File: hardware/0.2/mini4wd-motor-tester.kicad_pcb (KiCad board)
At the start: 4 copper layers, 100 x 48 mm, 116 parts, among them J1 USB_C_Receptacle_USB2.0_16P, J2 JST SH, J4 JST XH, M1 Motor_DC, M2 TP, M3 TP, Q2 AO3401A, Q3 2N7002, SW1 RA, SW2 RA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

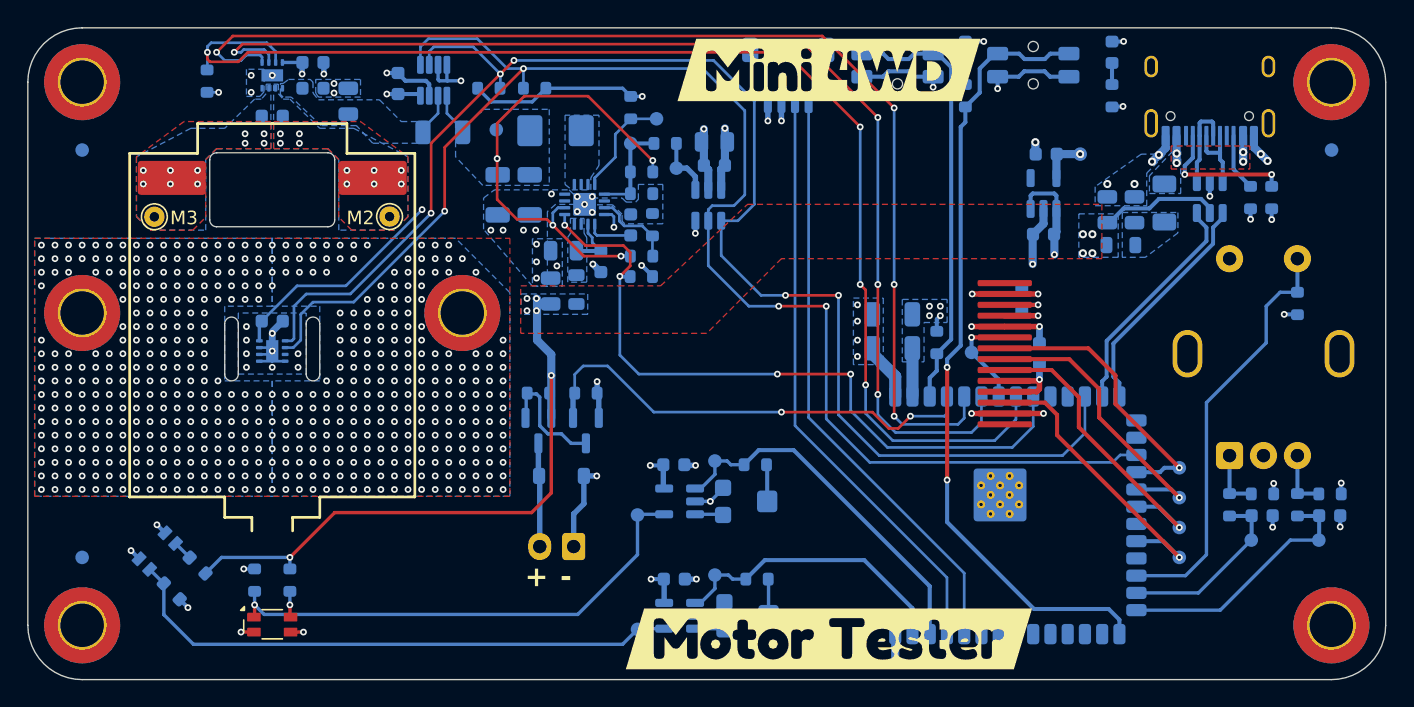
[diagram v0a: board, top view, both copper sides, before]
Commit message: add v2 heatsink, improve layout for v2 main
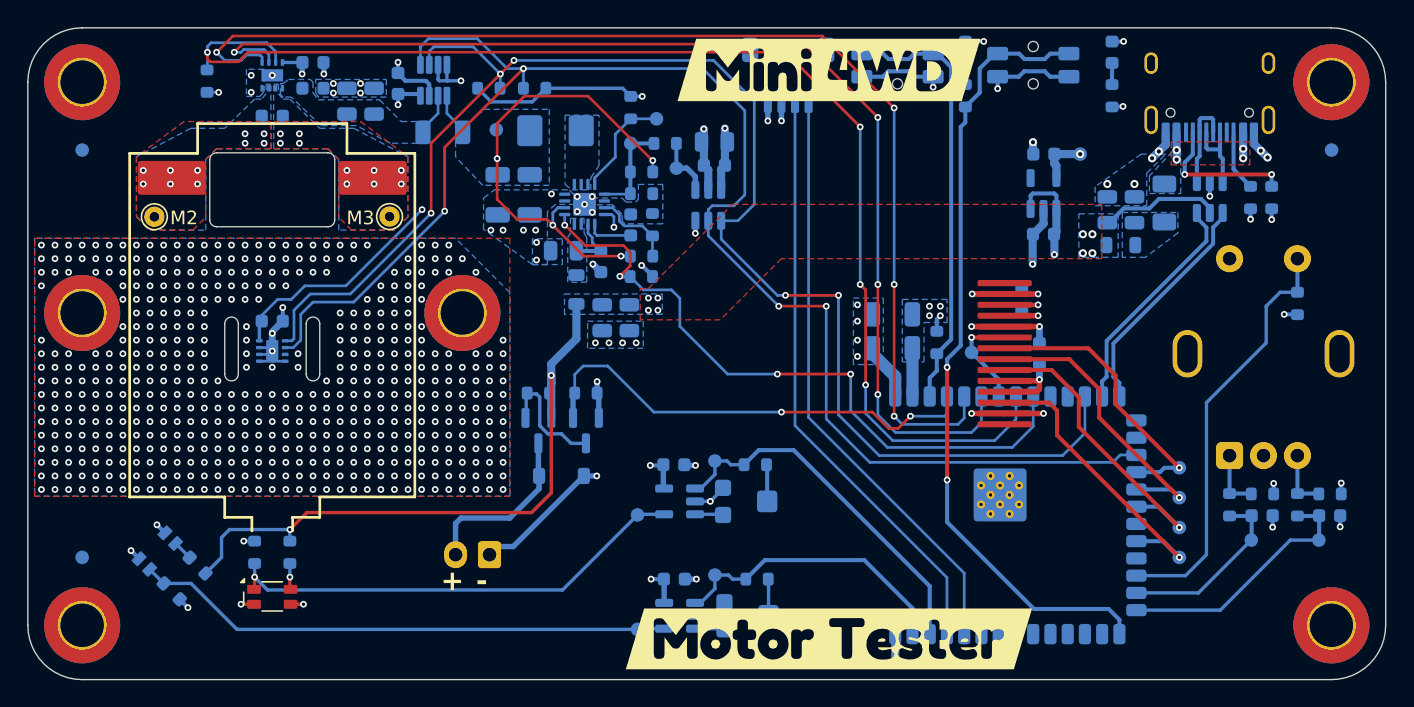
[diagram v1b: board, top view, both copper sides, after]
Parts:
- added C26: 10u, Capacitor_SMD:C_0805_2012Metric, B.Cu at (91.5, 81.4)
- added C27: 10u, Capacitor_SMD:C_0805_2012Metric, B.Cu at (110.3, 97.3)
- moved J4 6.23 mm to (100.0, 114.8)
- moved G1 6.17 mm to (86.8, 122.1)
- moved C1 4.28 mm to (108.3, 97.3), turned to -90 degrees
- moved R17 2.05 mm to (85.3, 114.6)
- moved R22 2.05 mm to (82.7, 114.6)
- moved U8 2.05 mm to (84.0, 118.0)
- moved J1 0.25 mm to (153.0, 79.7)
- moved C10 0.18 mm to (140.8, 85.3)
- moved C23 0.10 mm to (89.5, 81.4)
- renumbered M3 to M2, M2 to M3
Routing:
- net Net-(D3-K): track 7.64 -> 12.3 mm
- net GND: track 100.7 -> 105.3 mm, vias 594 -> 600
- net /REG_EN: track 52.8 -> 49.8 mm
- net Net-(U13--): track 37.1 -> 34.8 mm
- net Net-(U11--): track 42.0 -> 39.7 mm
- net +5V: track 63.1 -> 64.5 mm
- net /I2C_SCL: track 115.1 -> 113.8 mm
- net /I2C_SDA: track 111.5 -> 110.6 mm
- net +3V3: track 69.3 -> 69.8 mm
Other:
- board text added: "MINI4WD MOTOR TESTER REV 0.2"
- board text removed: "MINI4WD MOTOR TESTER REVISION 0.2"

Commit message: minor sch and pcb updates
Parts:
- moved D3 5.49 mm to (104.3, 114.4), turned to -90 degrees
- moved Q2 0.70 mm to (104.3, 105.7)
- moved Q3 0.70 mm to (107.8, 105.7)
- moved R27 0.70 mm to (107.8, 102.9)
- moved R28 0.70 mm to (104.3, 102.9)
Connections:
- C5 pad 1: Net-(C5-Pad1) -> Net-(U2-VBUS)
- F1 pad 2: Net-(C5-Pad1) -> Net-(U2-VBUS)
- FB2 pad 2: Net-(C5-Pad1) -> Net-(U2-VBUS)
- U2 pad 5: +5V -> Net-(U2-VBUS)
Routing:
- net +5V: track 64.5 -> 55.4 mm
- net +VMOT: track 37.2 -> 28.6 mm
- net Net-(U2-VBUS): track 0.00 -> 5.14 mm
- net GND: track 105.3 -> 100.7 mm
- net Net-(D3-K): track 12.3 -> 14.5 mm
- net Net-(J1-CC1): track 10.6 -> 12.3 mm
- net /REG_EN: track 49.8 -> 48.6 mm
- net /AUX_5V_EN: track 34.6 -> 33.9 mm
- added copper zone on B.Cu, net Net-(U2-VBUS)
- removed copper zone on B.Cu, net Net-(C5-Pad1)

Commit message: off to fab
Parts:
- R29, R32: value 180K -> 200K
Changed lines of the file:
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@@
 			)
 		)
-		(property "LCSC" ""
+		(property "LCSC" "C25803"
 			(at 0 0 0)
 			(unlocked yes)
@@
 			)
 		)
-		(property "MPN " ""
+		(property "MPN " "0603WAF1003T5E"
 			(at 0 0 0)
 			(unlocked yes)
@@
 			)
 		)
-		(property "LCSC" ""
+		(property "LCSC" "C4216"
 			(at 0 0 180)
 			(unlocked yes)
@@
 			)
 		)
-		(property "MPN " ""
+		(property "MPN " "0603WAF3302T5E"
 			(at 0 0 180)
 			(unlocked yes)
@@
 			)
 		)
-		(property "LCSC" ""
+		(property "LCSC" "C8218"
 			(at 0 0 270)
 			(unlocked yes)
@@
 			)
 		)
-		(property "MPN " ""
+		(property "MPN " "0603WAF2000T5E"
 			(at 0 0 270)
 			(unlocked yes)
@@
 			)
 		)
-		(property "Value" "180K"
+		(property "Value" "200K"
 			(at 0 -1.43 0)
 			(layer "B.Fab")
@@
 			)
 		)
+		(property "Manufacturer" "UNI-ROYAL"
+			(at 0 0 180)
+			(unlocked yes)
+			(layer "B.Fab")
+			(hide yes)
+			(effects
+				(font
+					(size 1 1)
+					(thickness 0.15)
+				)
+				(justify mirror)
+			)
+		)
+		(property "LCSC" "C25811"
+			(at 0 0 180)
+			(unlocked yes)
+			(layer "B.Fab")
+			(hide yes)
+			(effects
+				(font
+					(size 1 1)
+					(thickness 0.15)
+				)
+				(justify mirror)
+			)
+		)
+		(property "MPN " "0603WAF2003T5E"
+			(at 0 0 180)
+			(unlocked yes)
+			(layer "B.Fab")
+			(hide yes)
+			(effects
+				(font
+					(size 1 1)
+					(thickness 0.15)
+				)
+				(justify mirror)
+			)
+		)
 		(property ki_fp_filters "R_*")
 		(sheetname "/")
@@
 			)
 		)
-		(property "LCSC" ""
+		(property "LCSC" "C25819"
 			(at 0 0 90)
 			(unlocked yes)
@@
 			)
 		)
-		(property "MPN " ""
+		(property "MPN " "0603WAF4702T5E"
 			(at 0 0 90)
 			(unlocked yes)
@@
 			)
 		)
-		(property "LCSC" ""
+		(property "LCSC" "C157931"
 			(at 0 0 0)
 			(unlocked yes)
@@
 			)
 		)
-		(property "MPN " ""
+		(property "MPN " "S2B-XH-A(LF)(SN)"
 			(at 0 0 0)
 			(unlocked yes)
@@
 			)
 		)
-		(property "LCSC" ""
+		(property "LCSC" "C8218"
 			(at 0 0 135)
 			(unlocked yes)
@@
 			)
 		)
-		(property "MPN " ""
+		(property "MPN " "0603WAF2000T5E"
 			(at 0 0 135)
 			(unlocked yes)
@@
 			)
 		)
+		(property "LCSC" "C702117"
+			(at 0 0 180)
+			(unlocked yes)
+			(layer "B.Fab")
+			(hide yes)
+			(effects
+				(font
+					(size 1 1)
+					(thickness 0.15)
+				)
+				(justify mirror)
+			)
+		)
+		(property "MPN " "TLV7011DBVR"
+			(at 0 0 180)
+			(unlocked yes)
+			(layer "B.Fab")
+			(hide yes)
+			(effects
+				(font
+					(size 1 1)
+					(thickness 0.15)
+				)
+				(justify mirror)
+			)
+		)
+		(property "Manufacturer" "TI"
+			(at 0 0 180)
+			(unlocked yes)
+			(layer "B.Fab")
+			(hide yes)
+			(effects
+				(font
+					(size 1 1)
+					(thickness 0.15)
+				)
+				(justify mirror)
+			)
+		)
 		(property ki_fp_filters "SOT?23*")
 		(sheetname "/")
@@
 			)
 		)
-		(property "LCSC" ""
+		(property "LCSC" "C719186"
 			(at 0 0 180)
 			(unlocked yes)
@@
 			)
 		)
-		(property "LCSC" ""
+		(property "LCSC" "C719186"
 			(at 0 0 180)
 			(unlocked yes)
@@
 			)
 		)
-		(property "LCSC" ""
+		(property "LCSC" "C23186"
 			(at 0 0 270)
 			(unlocked yes)
@@
 			)
 		)
-		(property "MPN " ""
+		(property "MPN " "0603WAF5101T5E"
 			(at 0 0 270)
 			(unlocked yes)
@@
 			)
 		)
-		(property "Value" "180K"
+		(property "Value" "200K"
 			(at 0 -1.43 0)
 			(layer "B.Fab")
@@
 			)
 		)
+		(property "Manufacturer" "UNI-ROYAL"
+			(at 0 0 180)
+			(unlocked yes)
+			(layer "B.Fab")
+			(hide yes)
+			(effects
+				(font
+					(size 1 1)
+					(thickness 0.15)
+				)
+				(justify mirror)
+			)
+		)
+		(property "LCSC" "C25811"
+			(at 0 0 180)
+			(unlocked yes)
+			(layer "B.Fab")
+			(hide yes)
+			(effects
+				(font
+					(size 1 1)
+					(thickness 0.15)
+				)
+				(justify mirror)
+			)
+		)
+		(property "MPN " "0603WAF2003T5E"
+			(at 0 0 180)
+			(unlocked yes)
+			(layer "B.Fab")
+			(hide yes)
+			(effects
+				(font
+					(size 1 1)
+					(thickness 0.15)
+				)
+				(justify mirror)
+			)
+		)
 		(property ki_fp_filters "R_*")
 		(sheetname "/")
@@
 			)
 		)
+		(property "LCSC" "C702117"
+			(at 0 0 180)
+			(unlocked yes)
+			(layer "B.Fab")
+			(hide yes)
+			(effects
+				(font
+					(size 1 1)
+					(thickness 0.15)
+				)
+				(justify mirror)
+			)
+		)
+		(property "MPN " "TLV7011DBVR"
+			(at 0 0 180)
+			(unlocked yes)
+			(layer "B.Fab")
+			(hide yes)
+			(effects
+				(font
+					(size 1 1)
+					(thickness 0.15)
+				)
+				(justify mirror)
+			)
+		)
+		(property "Manufacturer" "TI"
+			(at 0 0 180)
+			(unlocked yes)
+			(layer "B.Fab")
+			(hide yes)
+			(effects
+				(font
+					(size 1 1)
+					(thickness 0.15)
+				)
+				(justify mirror)
+			)
+		)
 		(property ki_fp_filters "SOT?23*")
 		(sheetname "/")
@@
 			)
 		)
-		(property "LCSC" ""
+		(property "LCSC" "C25819"
 			(at 0 0 315)
 			(unlocked yes)
@@
 			)
 		)
-		(property "MPN " ""
+		(property "MPN " "0603WAF4702T5E"
 			(at 0 0 315)
 			(unlocked yes)
